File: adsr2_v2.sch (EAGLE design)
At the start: 55 parts, among them IC1 LM324D, IC2 4052D, SW1_TIME TL2285 L, SW2_TRIG TL2285 L, T1 BC847, T2 BC857, T3 BC857, T4 BC847, T5 BC857

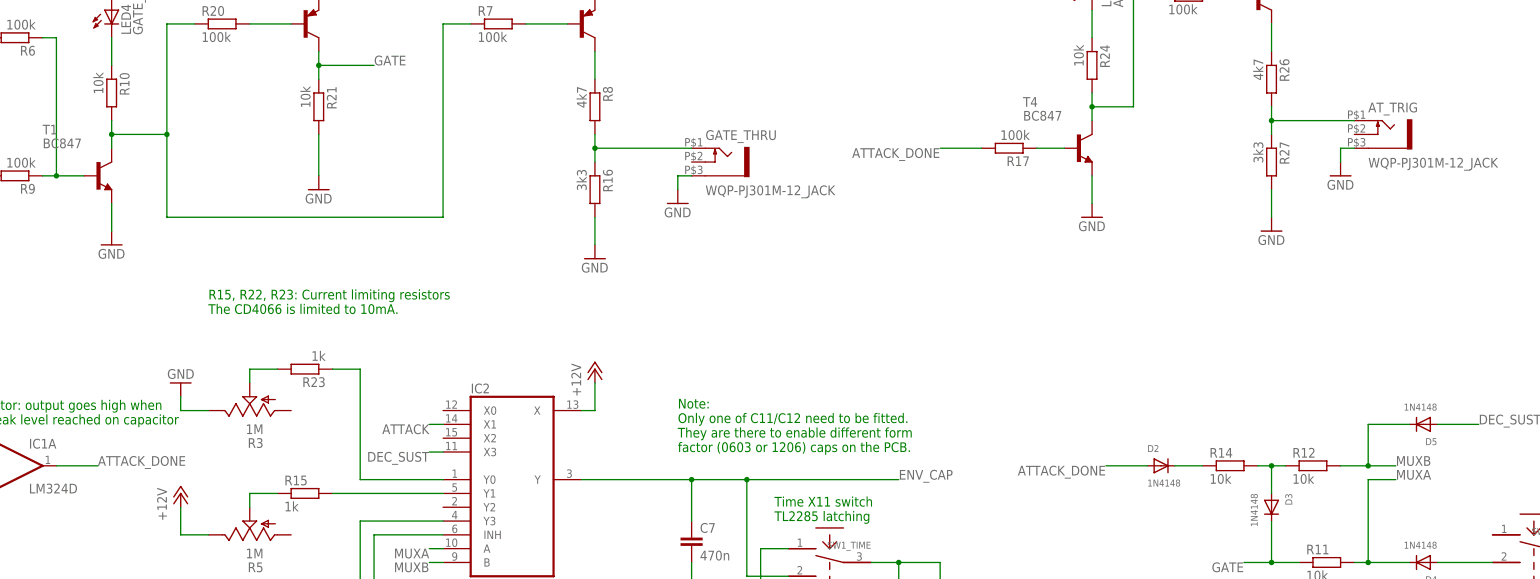
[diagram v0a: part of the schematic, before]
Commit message: Renamed comparator output net to "peak". Minor routing fixes on PCB.
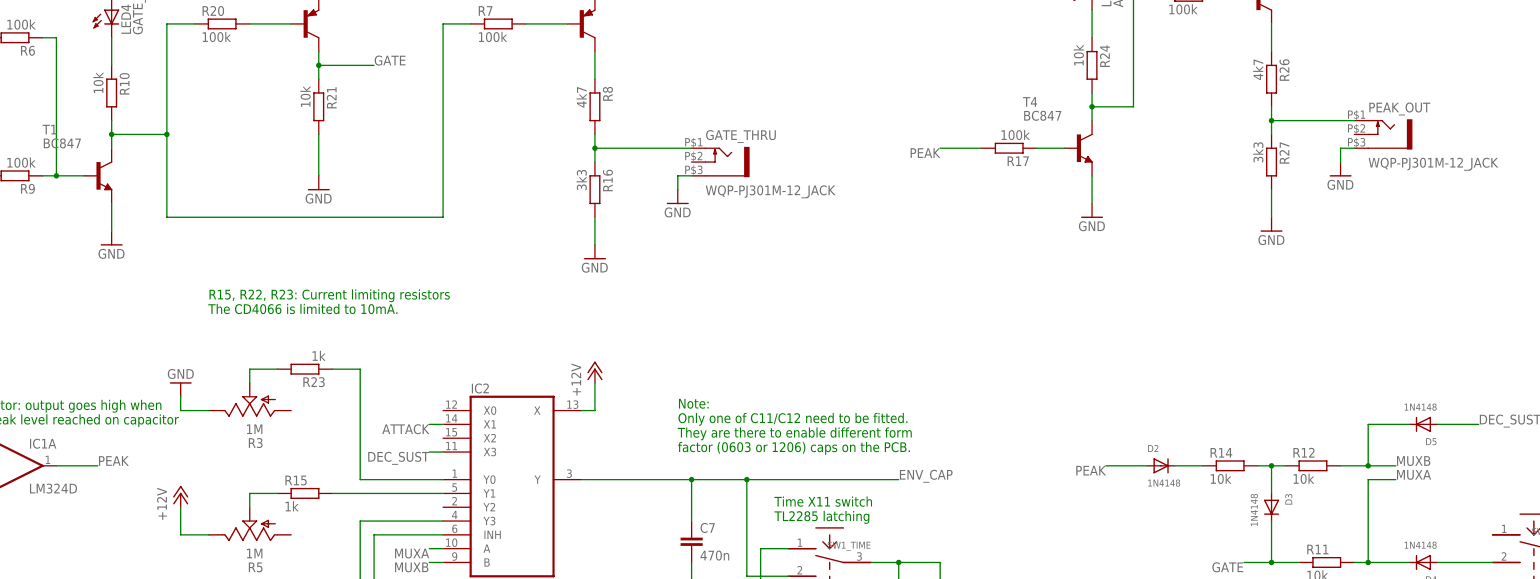
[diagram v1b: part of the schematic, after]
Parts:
- renumbered AT_TRIG to PEAK_OUT
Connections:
- net ATTACK_DONE renamed PEAK
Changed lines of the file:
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@@
 <part name="C12" library="rcl" deviceset="C-EU" device="C0603K" value="4u7"/>
 <part name="GND18" library="supply1" deviceset="GND" device=""/>
-<part name="AT_TRIG" library="thonkiconn" deviceset="WQP-PJ301M-12_JACK" device=""/>
+<part name="PEAK_OUT" library="thonkiconn" deviceset="WQP-PJ301M-12_JACK" device=""/>
 <part name="GND19" library="supply1" deviceset="GND" device=""/>
 <part name="R19" library="rcl" deviceset="R-EU_" device="R0603" value="10k"/>
@@
 <instance part="C12" gate="G$1" x="218.44" y="106.68"/>
 <instance part="GND18" gate="1" x="220.98" y="91.44"/>
-<instance part="AT_TRIG" gate="G$1" x="307.34" y="193.04"/>
+<instance part="PEAK_OUT" gate="G$1" x="307.34" y="193.04"/>
 <instance part="GND19" gate="1" x="299.72" y="185.42"/>
 <instance part="R19" gate="G$1" x="193.04" y="101.6" rot="R90"/>
@@
 </segment>
 <segment>
-<pinref part="AT_TRIG" gate="G$1" pin="1"/>
+<pinref part="PEAK_OUT" gate="G$1" pin="1"/>
 <wire x1="302.26" y1="190.5" x2="299.72" y2="190.5" width="0.1524" layer="91"/>
 <pinref part="GND19" gate="1" pin="GND"/>
@@
 </segment>
 </net>
-<net name="ATTACK_DONE" class="0">
+<net name="PEAK" class="0">
 <segment>
 <pinref part="IC1" gate="A" pin="OUT"/>
@@
 <pinref part="R27" gate="G$1" pin="1"/>
 <wire x1="287.02" y1="198.12" x2="287.02" y2="195.58" width="0.1524" layer="91"/>
-<pinref part="AT_TRIG" gate="G$1" pin="2"/>
+<pinref part="PEAK_OUT" gate="G$1" pin="2"/>
 <wire x1="287.02" y1="195.58" x2="287.02" y2="193.04" width="0.1524" layer="91"/>
 <wire x1="302.26" y1="195.58" x2="287.02" y2="195.58" width="0.1524" layer="91"/>

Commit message: Modified some text notes.
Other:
- note added: "R15, R22, R23: Current limiting resistors The switches in IC2 are limited to 10mA."
- note removed: "R15, R22, R23: Current limiting resistors The CD4066 is limited to 10mA."
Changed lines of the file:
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@@
 (press -&gt; triggered, always completes attack phase even if gate goes low/off)</text>
 <text x="43.18" y="104.14" size="1.778" layer="91">Sustain level buffer</text>
-<text x="43.18" y="139.7" size="1.778" layer="91">Comparator: output goes high when
+<text x="35.56" y="142.24" size="1.778" layer="91">Comparator: output goes high when
 attack peak level reached on capacitor</text>
-<text x="91.44" y="160.02" size="1.778" layer="91">R15, R22, R23: Current limiting resistors
-The CD4066 is limited to 10mA.</text>
+<text x="127" y="93.98" size="1.778" layer="91">R15, R22, R23: Current limiting resistors
+The switches in IC2 are limited to 10mA.</text>
 <text x="17.78" y="200.66" size="1.778" layer="91">TL2285 momentary
 Manual trigger button</text>

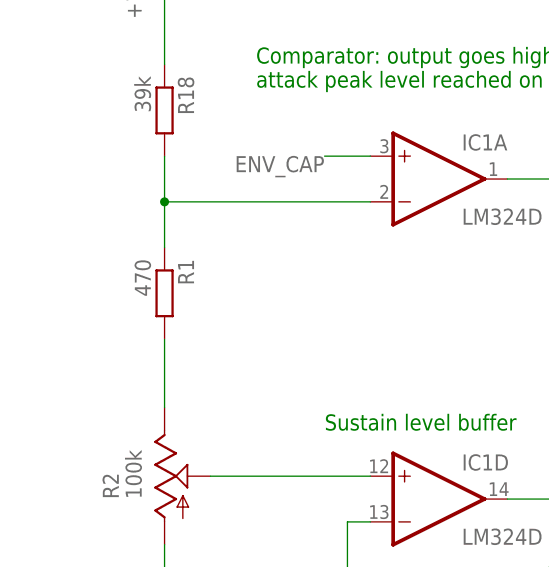
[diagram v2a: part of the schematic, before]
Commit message: Changed R1 to 1k.
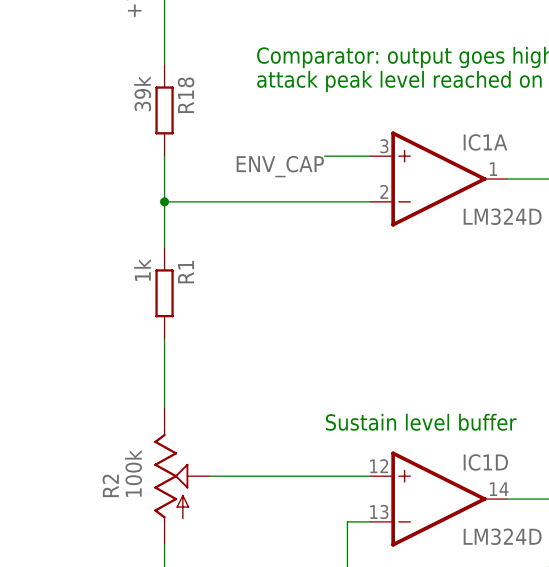
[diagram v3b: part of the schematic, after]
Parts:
- R1: value 470 -> 1k
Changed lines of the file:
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@@
 <part name="GND21" library="supply1" deviceset="GND" device=""/>
 <part name="P+2" library="supply1" deviceset="+12V" device=""/>
-<part name="R1" library="rcl" deviceset="R-EU_" device="R0603" value="470"/>
+<part name="R1" library="rcl" deviceset="R-EU_" device="R0603" value="1k"/>
 <part name="R18" library="rcl" deviceset="R-EU_" device="R0603" value="39k"/>
 <part name="P+3" library="supply1" deviceset="+12V" device=""/>

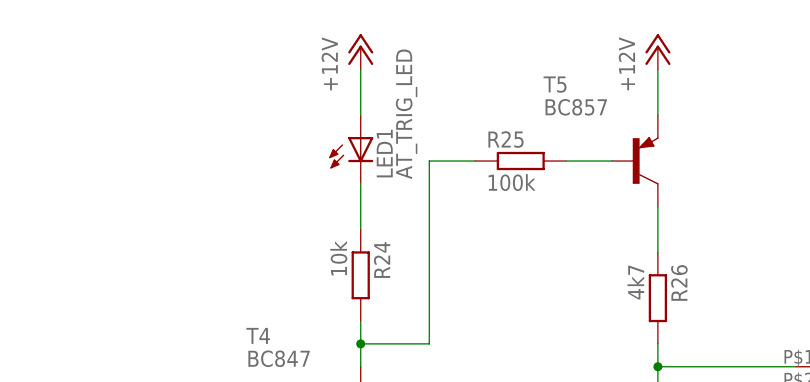
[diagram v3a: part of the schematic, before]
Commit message: Changed LEDs to 5mm footprint. Moved T3 and surrounding resistors a bit.
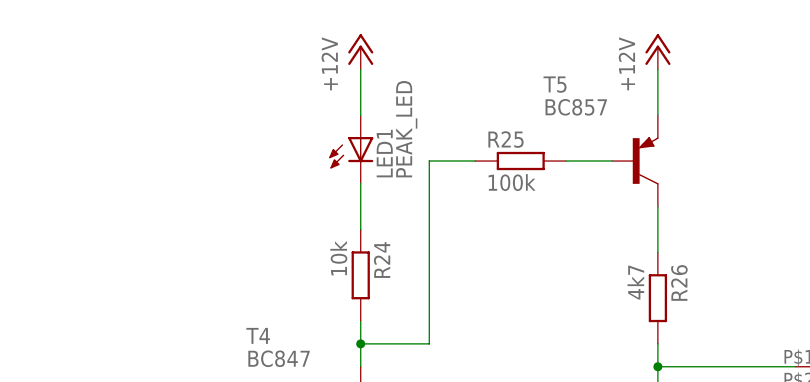
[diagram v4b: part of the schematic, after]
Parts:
- LED1: value AT_TRIG_LED -> PEAK_LED; device led:LED3MM -> led:LED5MM
- LED4: device led:LED3MM -> led:LED5MM
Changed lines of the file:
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@@
 <grid distance="0.1" unitdist="inch" unit="inch" style="lines" multiple="1" display="no" altdistance="0.01" altunitdist="inch" altunit="inch"/>
 <layers>
-<layer number="1" name="Top" color="4" fill="1" visible="no" active="no"/>
-<layer number="16" name="Bottom" color="1" fill="1" visible="no" active="no"/>
-<layer number="17" name="Pads" color="2" fill="1" visible="no" active="no"/>
-<layer number="18" name="Vias" color="2" fill="1" visible="no" active="no"/>
-<layer number="19" name="Unrouted" color="14" fill="1" visible="no" active="no"/>
-<layer number="20" name="Dimension" color="15" fill="1" visible="no" active="no"/>
-<layer number="21" name="tPlace" color="7" fill="1" visible="no" active="no"/>
-<layer number="22" name="bPlace" color="7" fill="1" visible="no" active="no"/>
-<layer number="23" name="tOrigins" color="15" fill="1" visible="no" active="no"/>
-<layer number="24" name="bOrigins" color="15" fill="1" visible="no" active="no"/>
-<layer number="25" name="tNames" color="7" fill="1" visible="no" active="no"/>
-<layer number="26" name="bNames" color="7" fill="1" visible="no" active="no"/>
-<layer number="27" name="tValues" color="7" fill="1" visible="no" active="no"/>
-<layer number="28" name="bValues" color="7" fill="1" visible="no" active="no"/>
+<layer number="1" name="Top" color="4" fill="1" visible="yes" active="no"/>
+<layer number="16" name="Bottom" color="1" fill="1" visible="yes" active="no"/>
+<layer number="17" name="Pads" color="2" fill="1" visible="yes" active="no"/>
+<layer number="18" name="Vias" color="2" fill="1" visible="yes" active="no"/>
+<layer number="19" name="Unrouted" color="14" fill="1" visible="yes" active="no"/>
+<layer number="20" name="Dimension" color="15" fill="1" visible="yes" active="no"/>
+<layer number="21" name="tPlace" color="7" fill="1" visible="yes" active="no"/>
+<layer number="22" name="bPlace" color="7" fill="1" visible="yes" active="no"/>
+<layer number="23" name="tOrigins" color="15" fill="1" visible="yes" active="no"/>
+<layer number="24" name="bOrigins" color="15" fill="1" visible="yes" active="no"/>
+<layer number="25" name="tNames" color="7" fill="1" visible="yes" active="no"/>
+<layer number="26" name="bNames" color="7" fill="1" visible="yes" active="no"/>
+<layer number="27" name="tValues" color="7" fill="1" visible="yes" active="no"/>
+<layer number="28" name="bValues" color="7" fill="1" visible="yes" active="no"/>
 <layer number="29" name="tStop" color="7" fill="3" visible="no" active="no"/>
 <layer number="30" name="bStop" color="7" fill="6" visible="no" active="no"/>
@@
 <layer number="35" name="tGlue" color="7" fill="4" visible="no" active="no"/>
 <layer number="36" name="bGlue" color="7" fill="5" visible="no" active="no"/>
-<layer number="37" name="tTest" color="7" fill="1" visible="no" active="no"/>
-<layer number="38" name="bTest" color="7" fill="1" visible="no" active="no"/>
+<layer number="37" name="tTest" color="7" fill="1" visible="yes" active="no"/>
+<layer number="38" name="bTest" color="7" fill="1" visible="yes" active="no"/>
 <layer number="39" name="tKeepout" color="4" fill="11" visible="no" active="no"/>
 <layer number="40" name="bKeepout" color="1" fill="11" visible="no" active="no"/>
@@
 <layer number="44" name="Drills" color="7" fill="1" visible="no" active="no"/>
 <layer number="45" name="Holes" color="7" fill="1" visible="no" active="no"/>
-<layer number="46" name="Milling" color="3" fill="1" visible="no" active="no"/>
-<layer number="47" name="Measures" color="7" fill="1" visible="no" active="no"/>
-<layer number="48" name="Document" color="7" fill="1" visible="no" active="no"/>
-<layer number="49" name="Reference" color="7" fill="1" visible="no" active="no"/>
-<layer number="50" name="dxf" color="7" fill="1" visible="no" active="no"/>
-<layer number="51" name="tDocu" color="7" fill="1" visible="no" active="no"/>
-<layer number="52" name="bDocu" color="7" fill="1" visible="no" active="no"/>
-<layer number="53" name="tGND_GNDA" color="7" fill="9" visible="no" active="no"/>
-<layer number="54" name="bGND_GNDA" color="1" fill="9" visible="no" active="no"/>
-<layer number="56" name="wert" color="7" fill="1" visible="no" active="no"/>
-<layer number="57" name="tCAD" color="7" fill="1" visible="no" active="no"/>
+<layer number="46" name="Milling" color="3" fill="1" visible="yes" active="no"/>
+<layer number="47" name="Measures" color="7" fill="1" visible="yes" active="no"/>
+<layer number="48" name="Document" color="7" fill="1" visible="yes" active="no"/>
+<layer number="49" name="Reference" color="7" fill="1" visible="yes" active="no"/>
+<layer number="50" name="dxf" color="7" fill="1" visible="yes" active="no"/>
+<layer number="51" name="tDocu" color="7" fill="1" visible="yes" active="no"/>
+<layer number="52" name="bDocu" color="7" fill="1" visible="yes" active="no"/>
+<layer number="53" name="tGND_GNDA" color="7" fill="9" visible="yes" active="no"/>
+<layer number="54" name="bGND_GNDA" color="1" fill="9" visible="yes" active="no"/>
+<layer number="56" name="wert" color="7" fill="1" visible="yes" active="no"/>
+<layer number="57" name="tCAD" color="7" fill="1" visible="yes" active="no"/>
 <layer number="90" name="Modules" color="5" fill="1" visible="yes" active="yes"/>
 <layer number="91" name="Nets" color="2" fill="1" visible="yes" active="yes"/>
@@
 <part name="IC1" library="linear" deviceset="LM324" device="D"/>
 <part name="P+5" library="supply1" deviceset="+12V" device=""/>
-<part name="LED4" library="led" deviceset="LED" device="3MM" value="GATE_LED"/>
+<part name="LED4" library="led" deviceset="LED" device="5MM" value="GATE_LED"/>
 <part name="R20" library="rcl" deviceset="R-EU_" device="R0603" value="100k"/>
 <part name="T2" library="transistor" deviceset="*-PNP-" device="SOT23-BEC" technology="BC857A" value="BC857"/>
@@
 <part name="T4" library="transistor" deviceset="BC847" device=""/>
 <part name="R24" library="rcl" deviceset="R-EU_" device="R0603" value="10k"/>
-<part name="LED1" library="led" deviceset="LED" device="3MM" value="AT_TRIG_LED"/>
+<part name="LED1" library="led" deviceset="LED" device="5MM" value="PEAK_LED"/>
 <part name="P+10" library="supply1" deviceset="+12V" device=""/>
 <part name="R25" library="rcl" deviceset="R-EU_" device="R0603" value="100k"/>
